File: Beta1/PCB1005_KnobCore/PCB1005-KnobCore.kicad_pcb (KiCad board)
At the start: 2 copper layers, 160 x 75.5 mm, 24 parts, among them J1 Axoloti_40Pin, J10 CON_1x4, J11 CON_1x4, J2 FPC_20POS, J20 CON_1x4, J21 CON_1x4, U2 MCP3008T-I/SL

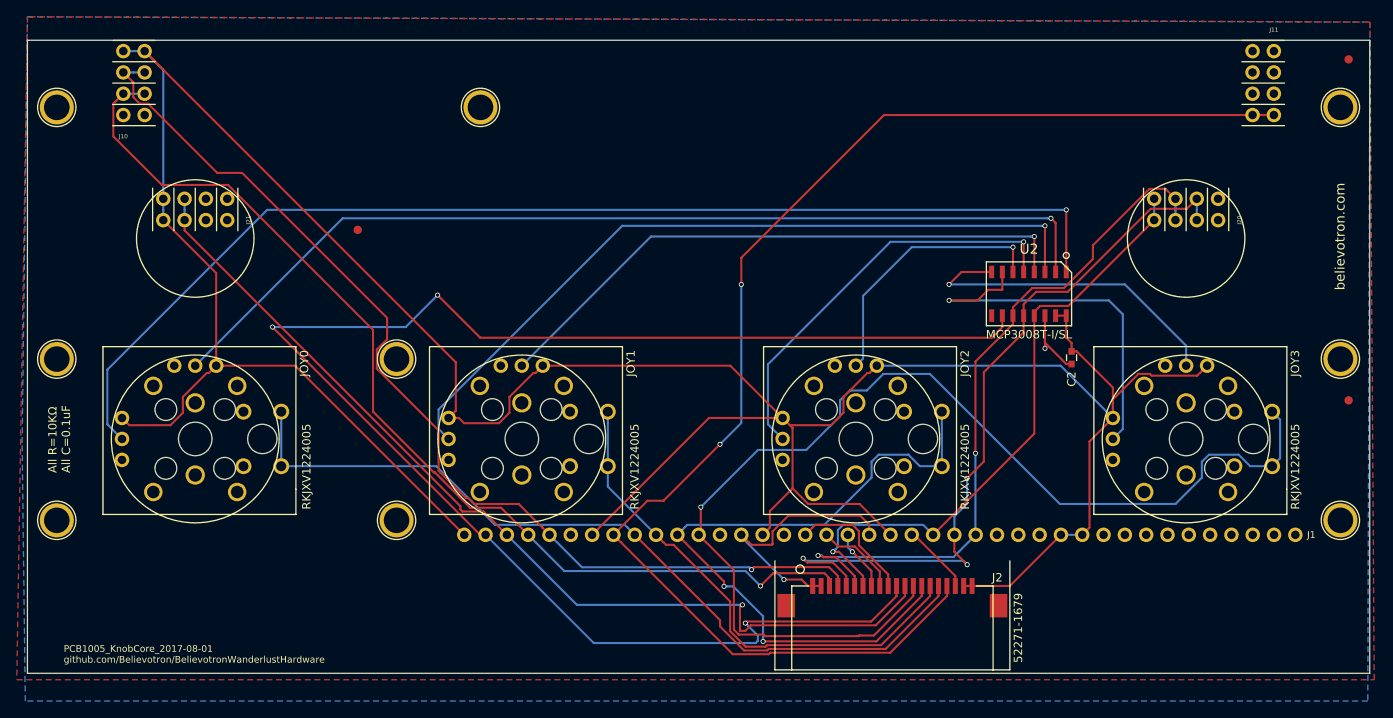
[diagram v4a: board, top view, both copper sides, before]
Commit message: Readded pots and OLED. Placement done
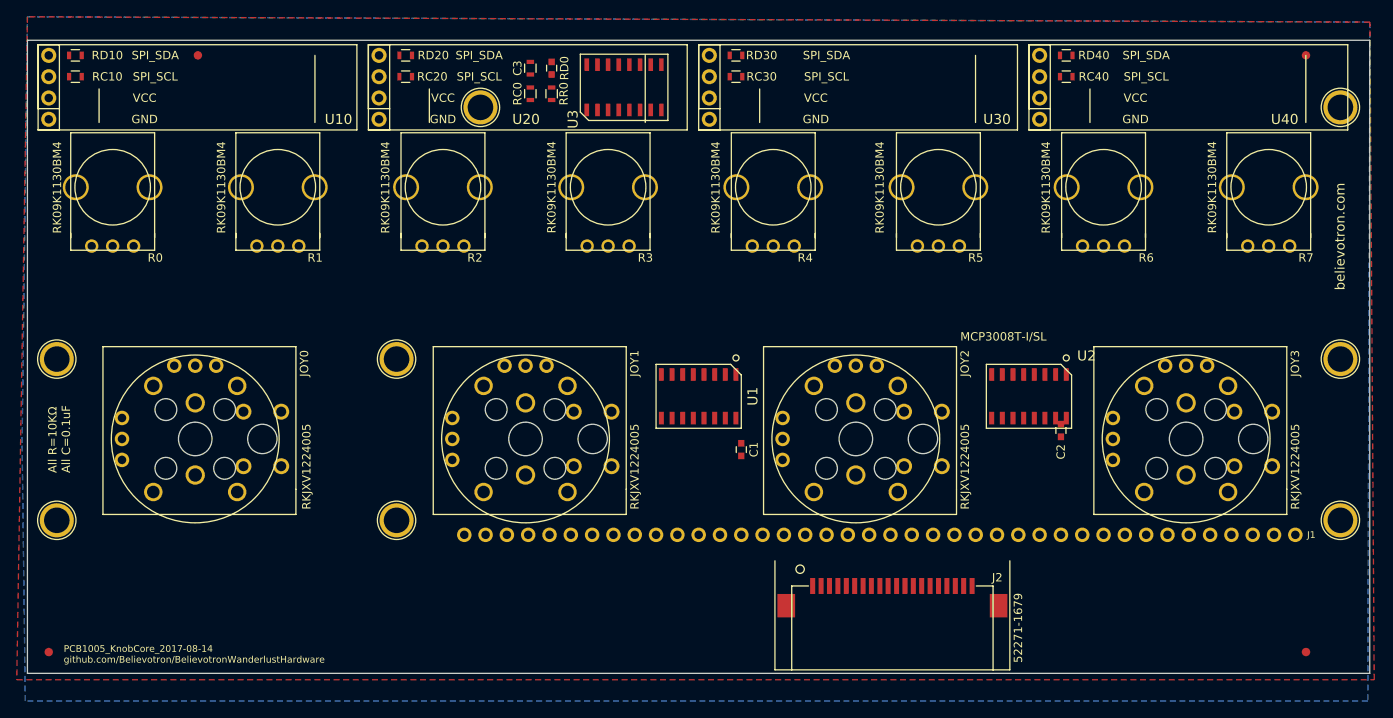
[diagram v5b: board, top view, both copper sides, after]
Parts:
- removed J10, J11: CON_1x4, Liberry:CON_0.1_x4_Double
- removed J20, J21: CON_1x4, Liberry:CON_0.1_x4_Double_Joy_symbol
- removed the REF** at (3.50, -52.2)
- added C1: 0.1u, Capacitors_SMD:C_0603, F.Cu at (85.1, -11.4)
- added C3: 0.1u, Capacitors_SMD:C_0603, F.Cu at (62.5, -56.9)
- added R0: POT, Liberry:POT_ALPS_RK09K1130BM4, F.Cu at (10.2, -42.7)
- added R1: POT, Liberry:POT_ALPS_RK09K1130BM4, F.Cu at (29.8, -42.7)
- added R2: POT, Liberry:POT_ALPS_RK09K1130BM4, F.Cu at (49.5, -42.7)
- added R3: POT, Liberry:POT_ALPS_RK09K1130BM4, F.Cu at (69.2, -42.7)
- added R4: POT, Liberry:POT_ALPS_RK09K1130BM4, F.Cu at (88.9, -42.7)
- added R5: POT, Liberry:POT_ALPS_RK09K1130BM4, F.Cu at (108.6, -42.7)
- added R6: POT, Liberry:POT_ALPS_RK09K1130BM4, F.Cu at (128.3, -42.7)
- added R7: POT, Liberry:POT_ALPS_RK09K1130BM4, F.Cu at (148.0, -42.7)
- added RC0: 10K, Resistors_SMD:R_0603, F.Cu at (59.9, -53.8)
- added RC10: 10K, Resistors_SMD:R_0603, F.Cu at (5.71, -55.9)
- added RC20: 10K, Resistors_SMD:R_0603, F.Cu at (45.1, -55.9)
- added RC30: 10K, Resistors_SMD:R_0603, F.Cu at (84.5, -55.9)
- added RC40: 10K, Resistors_SMD:R_0603, F.Cu at (123.8, -55.9)
- added RD0: 10K, Resistors_SMD:R_0603, F.Cu at (59.9, -56.9)
- added RD10: 10K, Resistors_SMD:R_0603, F.Cu at (5.71, -58.4)
- added RD20: 10K, Resistors_SMD:R_0603, F.Cu at (45.1, -58.4)
- added RD30: 10K, Resistors_SMD:R_0603, F.Cu at (84.5, -58.4)
- added RD40: 10K, Resistors_SMD:R_0603, F.Cu at (123.8, -58.4)
- added REF**: Fiducial_1mm_Dia_2.54mm_Outer_CopperBottom, Fiducials:Fiducial_1mm_Dia_2.54mm_Outer_CopperBottom, B.Cu at (2.54, 12.7)
- added RR0: 10K, Resistors_SMD:R_0603, F.Cu at (62.5, -53.8)
- added U1: MCP3008T-I/SL, Liberry:SOIC-16, F.Cu at (80.0, -17.8)
- added U10: OLED_128x32_I2C, Liberry:OLED_128x32, F.Cu at (2.54, -58.4)
- added U20: OLED_128x32_I2C, Liberry:OLED_128x32, F.Cu at (41.9, -58.4)
- added U3: I2C_1x4MUX_TCA9546A, Liberry:SOIC-16_1.27x5.4, F.Cu at (71.1, -54.6)
- added U30: OLED_128x32_I2C, Liberry:OLED_128x32, F.Cu at (81.3, -58.4)
- added U40: OLED_128x32_I2C, Liberry:OLED_128x32, F.Cu at (120.7, -58.4)
- moved REF** 30.4 mm to (152.4, 12.7)
- moved REF** 28.2 mm to (20.3, -58.4)
- moved U2 12.2 mm to (119.4, -17.8)
- moved C2 8.77 mm to (123.2, -13.7)
- moved REF** 5.10 mm to (152.4, -58.4)
- moved JOY1 0.44 mm to (59.4, -12.7)
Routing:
- net +3V3: track 370.1 -> 0.00 mm
- net /CS_8_15: track 189.4 -> 0.00 mm, vias 3 -> 0
- net /!OLED_RESET: track 160.7 -> 0.00 mm, vias 2 -> 0
- net /JOY_0_0: track 138.6 -> 0.00 mm, vias 1 -> 0
- net /JOY_3_SW: track 134.9 -> 0.00 mm, vias 1 -> 0
- net /I2C_SCL: track 123.2 -> 0.00 mm, vias 1 -> 0
- net /I2C_SDA: track 123.1 -> 0.00 mm, vias 1 -> 0
- net /JOY_0_1: track 115.9 -> 0.00 mm, vias 1 -> 0
- net /CS_0_7: track 114.7 -> 0.00 mm, vias 1 -> 0
- net /JOY_0_SW: track 98.3 -> 0.00 mm
- net /JOY_1_0: track 90.8 -> 0.00 mm, vias 1 -> 0
- net /SPI_MISO: track 90.6 -> 0.00 mm, vias 3 -> 0
- net /SPI_MOSI: track 84.7 -> 0.00 mm, vias 2 -> 0
- net /JOY_2_SW: track 83.6 -> 0.00 mm, vias 2 -> 0
- net /SPI_CLK: track 73.8 -> 0.00 mm, vias 1 -> 0
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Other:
- board text added: "PCB1005_KnobCore_2017-08-14 github.com/Believotron/BelievotronWanderlustHardware"
- board text removed: "PCB1005_KnobCore_2017-08-01 github.com/Believotron/BelievotronWanderlustHardware"

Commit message: mid route
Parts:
- moved C2 1.69 mm to (124.0, -12.2)
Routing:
- net /JOY_0_0: track 0.00 -> 127.5 mm, vias 0 -> 2
- net /I2C_SCL: track 0.00 -> 116.6 mm, vias 0 -> 2
- net /JOY_0_1: track 0.00 -> 116.5 mm
- net /SPI_MOSI: track 0.00 -> 89.9 mm, vias 0 -> 3
- net /SPI_MISO: track 0.00 -> 89.8 mm, vias 0 -> 3
- net /JOY_1_0: track 0.00 -> 88.7 mm
- net /I2C_SDA: track 0.00 -> 82.0 mm, vias 0 -> 2
- net /SPI_CLK: track 0.00 -> 80.2 mm
- net /I2C_SCL0: track 0.00 -> 76.1 mm, vias 0 -> 2
- net /I2C_SDA0: track 0.00 -> 75.0 mm, vias 0 -> 2
- net /P0: track 0.00 -> 71.7 mm
- net /JOY_1_1: track 0.00 -> 70.0 mm
- net /P7: track 0.00 -> 69.8 mm
- net /I2C_SCL3: track 0.00 -> 59.2 mm
- net /I2C_SDA3: track 0.00 -> 57.5 mm
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
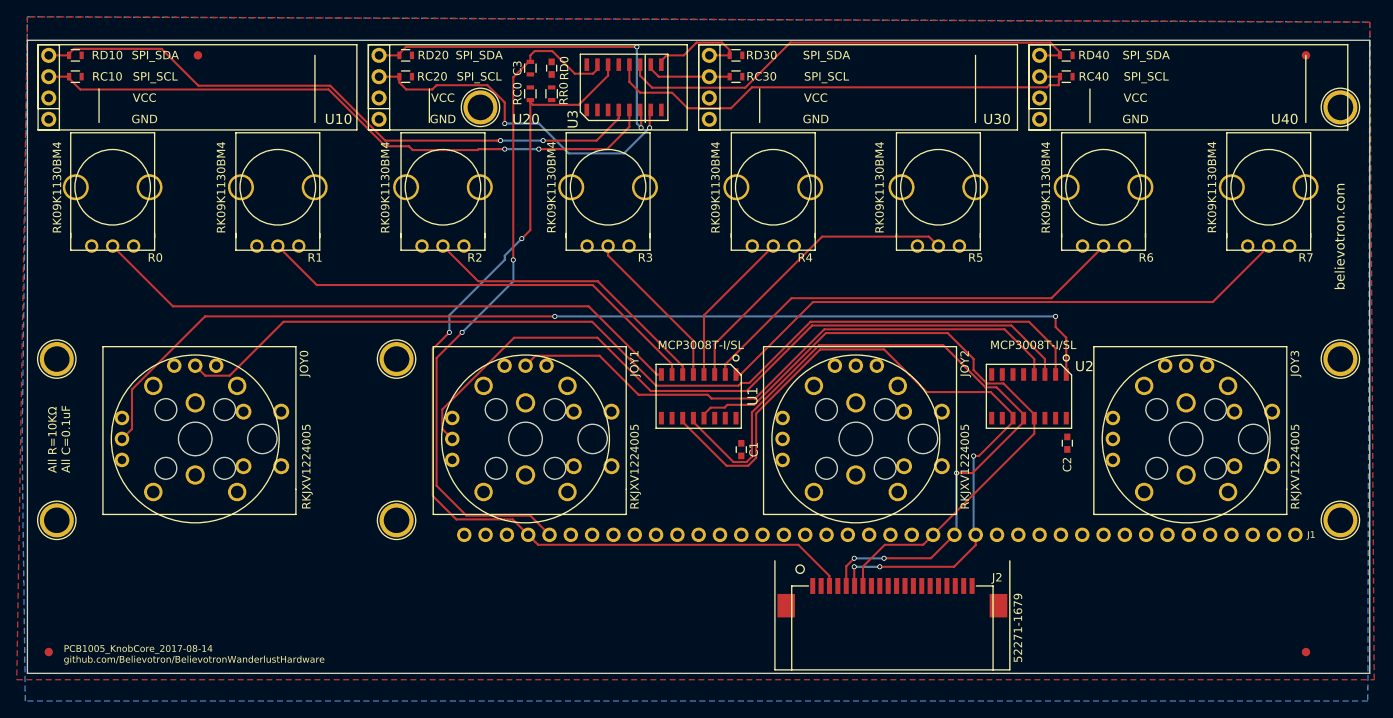
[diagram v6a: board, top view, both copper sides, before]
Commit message: Added Knobs + OLED back to PCB1005. Ready for Fab
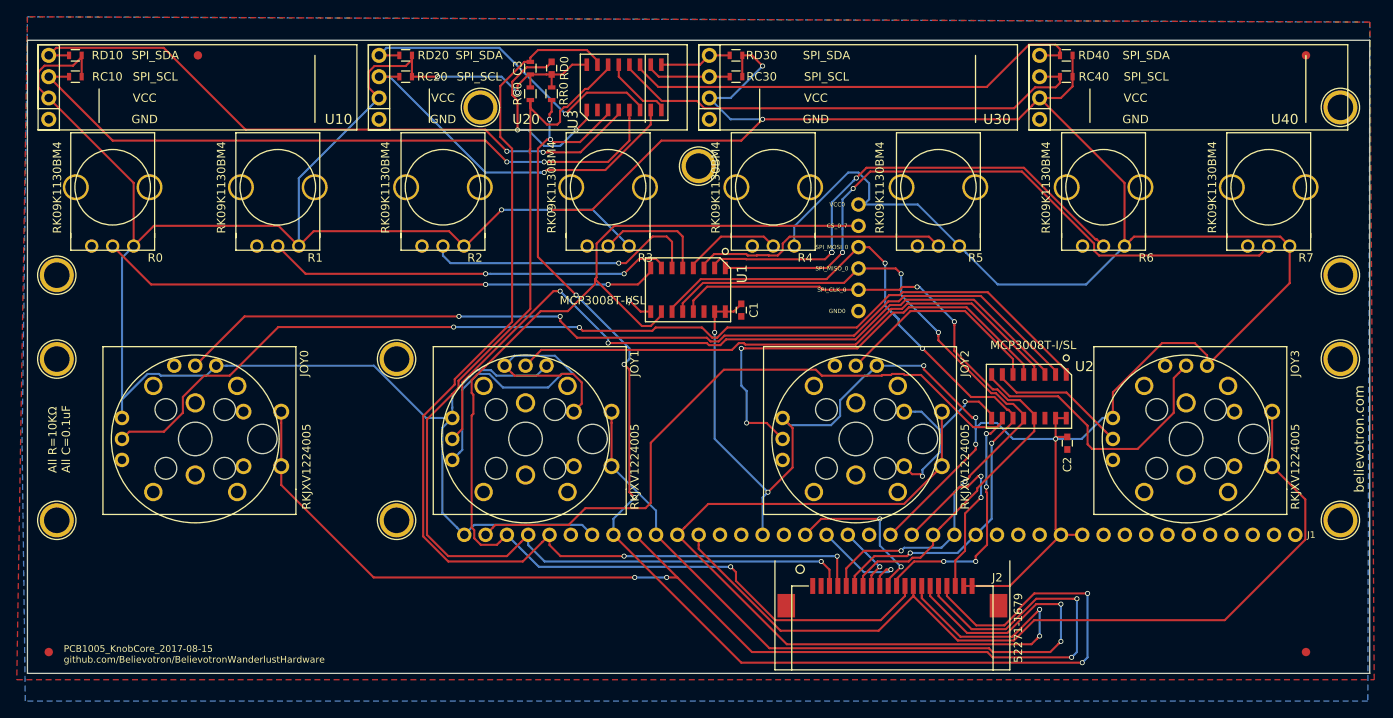
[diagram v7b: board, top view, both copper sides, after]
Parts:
- added CS_0_7: CONN_01X01, Liberry:single_0.1, F.Cu at (99.1, -38.1)
- added GND0: CONN_01X01, Liberry:single_0.1, F.Cu at (99.1, -27.9)
- added REF**: 1pin, Connect:1pin, F.Cu at (80.0, -45.2)
- added REF**: 1pin, Connect:1pin, F.Cu at (3.50, -32.2)
- added REF**: 1pin, Connect:1pin, F.Cu at (156.5, -32.2)
- added SPI_CLK_0: CONN_01X01, Liberry:single_0.1, F.Cu at (99.1, -30.5)
- added SPI_MISO_0: CONN_01X01, Liberry:single_0.1, F.Cu at (99.1, -33.0)
- added SPI_MOSI_0: CONN_01X01, Liberry:single_0.1, F.Cu at (99.1, -35.6)
- added VCC0: CONN_01X01, Liberry:single_0.1, F.Cu at (99.1, -40.6)
- moved C1 16.6 mm to (85.1, -28.1)
- moved U1 12.8 mm to (78.7, -30.5)
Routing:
- net +3V3: track 0.00 -> 647.5 mm, vias 0 -> 12
- net /!OLED_RESET: track 0.00 -> 159.9 mm, vias 0 -> 7
- net /JOY_0_SW: track 0.00 -> 146.7 mm, vias 0 -> 4
- net /CS_0_7: track 0.00 -> 146.2 mm, vias 0 -> 1
- net /JOY_2_SW: track 0.00 -> 112.3 mm, vias 0 -> 2
- net /CS_8_15: track 0.00 -> 107.1 mm, vias 0 -> 4
- net GND: track 0.00 -> 105.7 mm, vias 0 -> 5
- net /JOY_3_SW: track 0.00 -> 105.0 mm
- net /JOY_1_SW: track 0.00 -> 95.9 mm, vias 0 -> 2
- net /JOY_2_0: track 0.00 -> 53.9 mm, vias 0 -> 2
- net /I2C_SDA: track 82.0 -> 130.6 mm
- net /JOY_3_1: track 0.00 -> 34.9 mm
- net /JOY_2_1: track 0.00 -> 25.6 mm
- net /ANALOG_OUT: track 0.00 -> 25.5 mm, vias 0 -> 2
- net /VOLUME: track 0.00 -> 19.4 mm, vias 0 -> 2
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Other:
- board text added: "PCB1005_KnobCore_2017-08-15 github.com/Believotron/BelievotronWanderlustHardware"
- board text removed: "PCB1005_KnobCore_2017-08-14 github.com/Believotron/BelievotronWanderlustHardware"
